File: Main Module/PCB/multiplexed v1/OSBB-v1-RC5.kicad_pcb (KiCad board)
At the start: 2 copper layers, 85.6 x 49.8 mm, 170 parts, among them P1 AUX 1-3, P14 EXTRA Pins, P2 Wire to Teensy VUSB, P3 +3.3V, P4 Pit, P5 Encoders, P6 BTN 1-32, Q1 NPN, Q2 NPN, Q3 NPN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

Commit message: + moved position of label box
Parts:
- moved Ref** 16.0 mm to (243.1, 132.2)
- moved Ref** 15.1 mm to (240.8, 132.2)
- moved Ref** 3.81 mm to (225.9, 130.7)
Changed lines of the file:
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@@
     (area 175.269999 88.074999 261.407144 151.803575)
     (thickness 1.6)
-    (drawings 97)
+    (drawings 96)
     (tracks 1158)
     (zones 0)
@@
   )
   (module MOBB-KiCad-Lib:VIA-W0.6mm-H0.4mm (layer F.Cu)
-    (at 227.35 127.16)
+    (at 225.95 130.7)
     (fp_text reference Ref** (at 0 0.5) (layer F.Fab) hide
       (effects (font (size 0.127 0.127) (thickness 0.000001)))
@@
   )
   (module MOBB-KiCad-Lib:VIA-W0.6mm-H0.4mm (layer F.Cu)
-    (at 227.12 131.35)
+    (at 243.11 132.24)
     (fp_text reference Ref** (at 0 0.5) (layer F.Fab) hide
       (effects (font (size 0.127 0.127) (thickness 0.000001)))
@@
   )
   (module MOBB-KiCad-Lib:VIA-W0.6mm-H0.4mm (layer F.Cu)
-    (at 225.9 129.8)
+    (at 240.76 132.24)
     (fp_text reference Ref** (at 0 0.5) (layer F.Fab) hide
       (effects (font (size 0.127 0.127) (thickness 0.000001)))
@@
       (net 6 GND) (zone_connect 2))
   )
+  (gr_line (start 227.28 132.24) (end 227.28 129.5) (angle 90) (layer F.Fab) (width 0.2))
+  (gr_line (start 239.14 132.24) (end 227.28 132.24) (angle 90) (layer F.Fab) (width 0.2))
+  (gr_line (start 239.14 129.5) (end 239.14 132.24) (angle 90) (layer F.Fab) (width 0.2))
+  (gr_line (start 227.28 129.5) (end 239.14 129.5) (angle 90) (layer F.Fab) (width 0.2))
   (gr_text S (at 260.1 101.575) (layer F.SilkS)
     (effects (font (size 1 1) (thickness 0.25)))
@@
     (effects (font (size 1 1) (thickness 0.25)))
   )
-  (gr_line (start 243.57 130.3) (end 243.57 130.42) (angle 90) (layer F.Fab) (width 0.2))
-  (gr_line (start 228.33 130.3) (end 243.57 130.3) (angle 90) (layer F.Fab) (width 0.2))
-  (gr_line (start 228.33 133.35) (end 228.33 130.3) (angle 90) (layer F.Fab) (width 0.2))
-  (gr_line (start 243.54 133.35) (end 228.33 133.35) (angle 90) (layer F.Fab) (width 0.2))
-  (gr_line (start 243.54 130.3) (end 243.54 133.35) (angle 90) (layer F.Fab) (width 0.2))
   (gr_text VUSB (at 199.025 137.925) (layer F.SilkS)
     (effects (font (size 1 1) (thickness 0.2)))

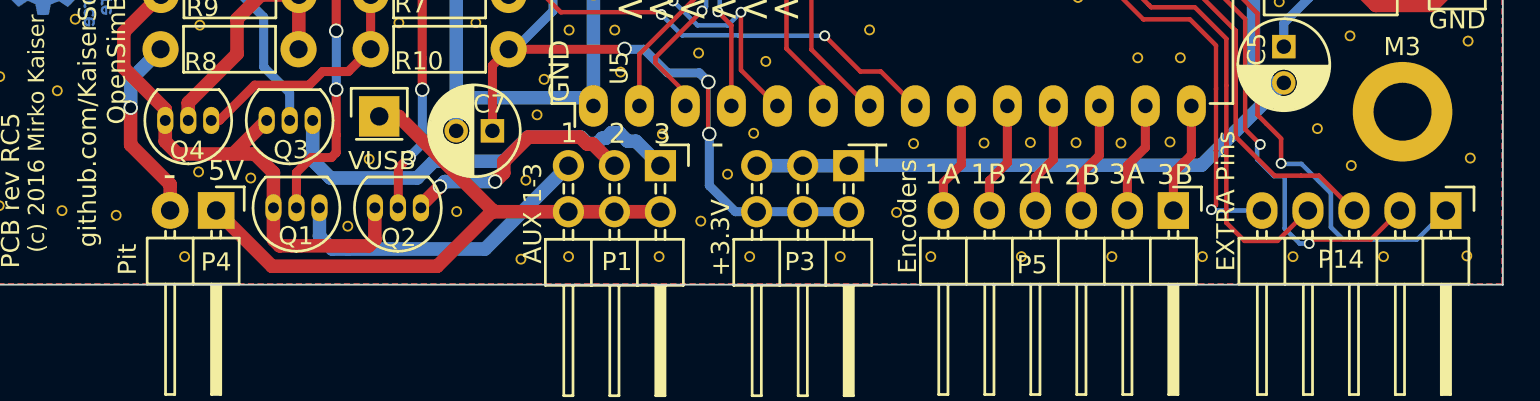
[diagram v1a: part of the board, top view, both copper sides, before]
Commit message: * added a few labels since I don't export all vlues for the gerber files * gerber files for RC5
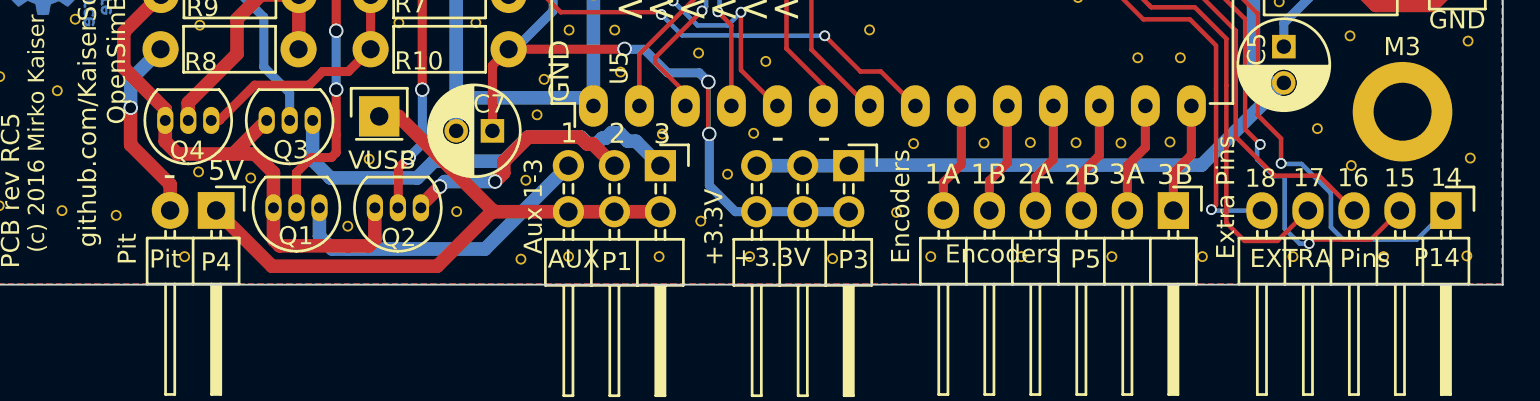
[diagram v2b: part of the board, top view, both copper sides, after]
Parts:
- P1: value AUX 1-3 -> AUX
- moved Ref** 0.43 mm to (223.9, 143.3)
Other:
- board text added: "+3.3V"
- board text added: "Aux 1-3"
- board text added: "Encoders"
- board text added: "Extra Pins"
- board text added: "Pit"
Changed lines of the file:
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@@
     (area 175.269999 88.074999 261.407144 151.803575)
     (thickness 1.6)
-    (drawings 96)
+    (drawings 106)
     (tracks 1158)
     (zones 0)
@@
       (drillshape 0)
       (scaleselection 1)
-      (outputdirectory ../Gerber-rev-RC4/))
+      (outputdirectory OSBB-v1-RC5/))
   )
   (net 0 "")
@@
   )
   (module MOBB-KiCad-Lib:VIA-W0.6mm-H0.4mm (layer F.Cu)
-    (at 224.33 143.22)
+    (at 223.91 143.33)
     (fp_text reference Ref** (at 0 0.5) (layer F.Fab) hide
       (effects (font (size 0.127 0.127) (thickness 0.000001)))
@@
       (effects (font (size 1 1) (thickness 0.15)))
     )
-    (fp_text value Pit (at 2.705 4.895 270) (layer F.SilkS)
+    (fp_text value Pit (at 2.69 2.82 360) (layer F.SilkS)
       (effects (font (size 1 1) (thickness 0.15)))
     )
@@
     (descr "Through hole pin header")
     (tags "pin header")
-    (fp_text reference P5 (at 3 7.8 360) (layer F.SilkS)
+    (fp_text reference P5 (at 2.685 4.845 360) (layer F.SilkS)
       (effects (font (size 1 1) (thickness 0.15)))
     )
-    (fp_text value Encoders (at 0.325 14.675 270) (layer F.SilkS)
+    (fp_text value Encoders (at 2.405 9.455 360) (layer F.SilkS)
       (effects (font (size 1 1) (thickness 0.15)))
     )
@@
       (effects (font (size 1 1) (thickness 0.15)))
     )
-    (fp_text value "AUX 1-3" (at 2.625 7.05 270) (layer F.SilkS)
+    (fp_text value AUX (at 5.16 4.78 360) (layer F.SilkS)
       (effects (font (size 1 1) (thickness 0.15)))
     )
@@
     (descr "Through hole pin header")
     (tags "pin header")
-    (fp_text reference P3 (at 5.3 2.7 360) (layer F.SilkS)
+    (fp_text reference P3 (at 5.19 -0.26 360) (layer F.SilkS)
       (effects (font (size 1 1) (thickness 0.15)))
     )
-    (fp_text value +3.3V (at 3.975 7.075 270) (layer F.SilkS)
+    (fp_text value +3.3V (at 5.07 4.23 360) (layer F.SilkS)
       (effects (font (size 1 1) (thickness 0.15)))
     )
@@
     (descr "Through hole pin header")
     (tags "pin header")
-    (fp_text reference P14 (at 2.7 5.8 360) (layer F.SilkS)
+    (fp_text reference P14 (at 2.605 0.505 360) (layer F.SilkS)
       (effects (font (size 1 1) (thickness 0.15)))
     )
-    (fp_text value "EXTRA Pins" (at -0.525 12.15 270) (layer F.SilkS)
+    (fp_text value "EXTRA Pins" (at 2.655 6.955 360) (layer F.SilkS)
       (effects (font (size 1 1) (thickness 0.15)))
     )
@@
       (net 6 GND) (zone_connect 2))
   )
+  (gr_text 14 (at 257.8 138.85) (layer F.SilkS)
+    (effects (font (size 1 1) (thickness 0.25)))
+  )
+  (gr_text 15 (at 255.22 138.88) (layer F.SilkS)
+    (effects (font (size 1 1) (thickness 0.25)))
+  )
+  (gr_text 16 (at 252.65 138.87) (layer F.SilkS)
+    (effects (font (size 1 1) (thickness 0.25)))
+  )
+  (gr_text 17 (at 250.21 138.87) (layer F.SilkS)
+    (effects (font (size 1 1) (thickness 0.25)))
+  )
+  (gr_text 18 (at 247.54 138.9) (layer F.SilkS)
+    (effects (font (size 1 1) (thickness 0.25)))
+  )
+  (gr_text "Extra Pins" (at 245.62 139.95 90) (layer F.SilkS)
+    (effects (font (size 1 1) (thickness 0.25)))
+  )
+  (gr_text Encoders (at 227.67 140.45 90) (layer F.SilkS)
+    (effects (font (size 1 1) (thickness 0.25)))
+  )
+  (gr_text +3.3V (at 217.36 141.6 90) (layer F.SilkS)
+    (effects (font (size 1 1) (thickness 0.25)))
+  )
+  (gr_text "Aux 1-3" (at 207.39 140.44 90) (layer F.SilkS)
+    (effects (font (size 1 1) (thickness 0.25)))
+  )
+  (gr_text Pit (at 184.97 142.8 90) (layer F.SilkS)
+    (effects (font (size 1 1) (thickness 0.25)))
+  )
   (gr_line (start 227.28 132.24) (end 227.28 129.5) (angle 90) (layer F.Fab) (width 0.2))
   (gr_line (start 239.14 132.24) (end 227.28 132.24) (angle 90) (layer F.Fab) (width 0.2))
@@
     (effects (font (size 1.2 1.2) (thickness 0.25)) (justify mirror))
   )
-  (gr_text - (at 226.65 136.925) (layer F.SilkS)
+  (gr_text - (at 223.44 136.61) (layer F.SilkS)
     (effects (font (size 1.5 1.5) (thickness 0.3)))
   )
-  (gr_text - (at 217.55 136.925) (layer F.SilkS)
+  (gr_text - (at 220.88 136.61) (layer F.SilkS)
     (effects (font (size 1.5 1.5) (thickness 0.3)))
   )
@@
     (effects (font (size 1 1) (thickness 0.25)))
   )
-  (gr_text VUSB (at 199.025 137.925) (layer F.SilkS)
+  (gr_text VUSB (at 199.03 137.9) (layer F.SilkS)
     (effects (font (size 1 1) (thickness 0.2)))
   )
